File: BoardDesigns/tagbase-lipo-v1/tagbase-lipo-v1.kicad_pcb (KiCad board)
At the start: 2 copper layers, 50.8 x 69.9 mm, 38 parts, among them J1 Conn_01x04_Female, J101 Conn_02x03_Odd_Even, J102 Conn_02x05_Odd_Even, J104 USB_B_Mini, J2 Conn_01x06, J5 Conn_01x02, SW1 SW_SPDT, SW2 SW_SPDT, U1 XC6206P332MR, U105 Tactile Switch, U2 XC6808ANC28R-G, U3 XC6206P182MR, U4 STM32C071GBUx, U5 SN74LVC1T45DCK, U6 SN74LVC1T45DCK

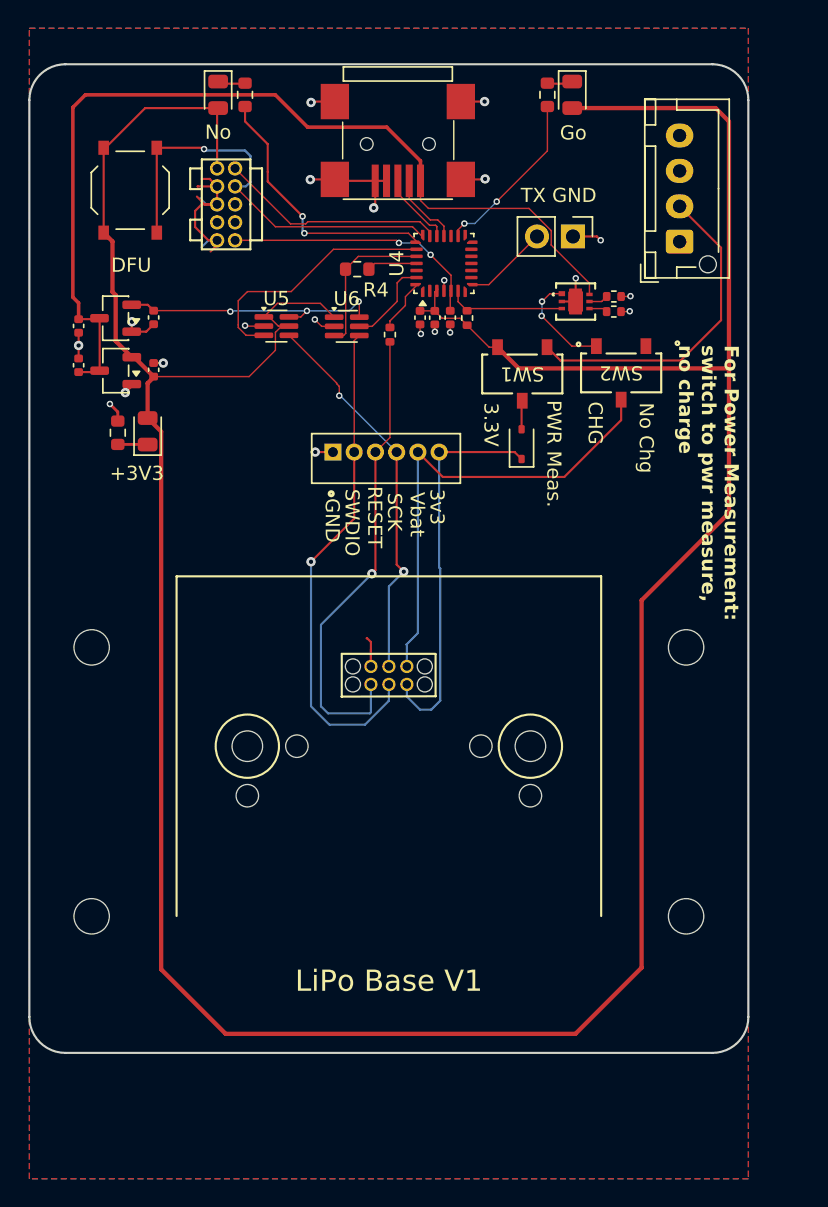
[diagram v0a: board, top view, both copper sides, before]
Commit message: added imutag with bmp581, bitprestag with bmp585
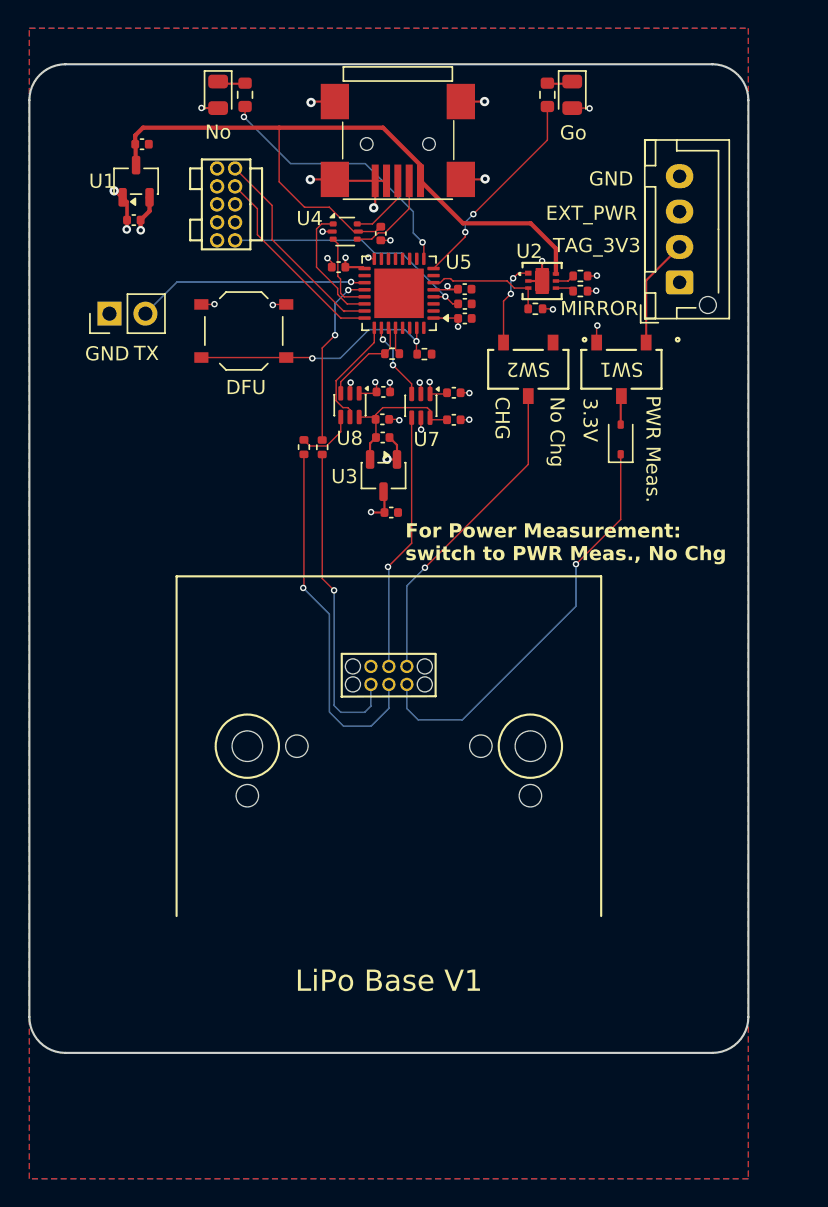
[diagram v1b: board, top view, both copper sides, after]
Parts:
- removed C101: 0.1uF, Capacitor_SMD:C_0402_1005Metric
- removed C6: 4.7uf, Capacitor_SMD:C_0402_1005Metric
- removed D105: LED-GREEN, Diode_SMD:D_0805_2012Metric
- removed H1, H2, H3, H4: MountingHole, MountingHole:MountingHole_2.5mm
- removed J2: Conn_01x06, tagbase:JST_B6B-ZR(LF)(SN)
- removed R5: 100, Resistor_SMD:R_0603_1608Metric
- removed U6: SN74LVC1T45DCK, Package_TO_SOT_SMD:SOT-363_SC-70-6
- added C102: 0.1uF, Capacitor_SMD:C_0402_1005Metric, F.Cu at (126.4, 62.8)
- added C103: 0.1uF, Capacitor_SMD:C_0402_1005Metric, F.Cu at (126.5, 75.9)
- added C109: 0.1uF, Capacitor_SMD:C_0402_1005Metric, F.Cu at (131.6, 75.9)
- added C110: 0.1uF, Capacitor_SMD:C_0402_1005Metric, F.Cu at (131.6, 74.0)
- added C111: 0.1uF, Capacitor_SMD:C_0402_1005Metric, F.Cu at (126.6, 74.0)
- added C3: 0.1uF, Capacitor_SMD:C_0402_1005Metric, F.Cu at (123.4, 65.1)
- added C7: 0.1uF, Capacitor_SMD:C_0402_1005Metric, F.Cu at (132.4, 67.7)
- added C8: 0.1uF, Capacitor_SMD:C_0402_1005Metric, F.Cu at (132.4, 66.7)
- added R105: 12K, Resistor_SMD:R_0402_1005Metric, F.Cu at (129.5, 71.3)
- added R106: 100, Resistor_SMD:R_0402_1005Metric, F.Cu at (121.0, 77.8)
- added U7: SN74LVC1T45DCK, Package_TO_SOT_SMD:SOT-363_SC-70-6, F.Cu at (129.3, 74.9)
- added U8: SN74LVC1T45DCK, Package_TO_SOT_SMD:SOT-363_SC-70-6, F.Cu at (124.2, 74.9)
- R102: value 100 -> 220
- R4: footprint Resistor_SMD:R_0603_1608Metric -> Resistor_SMD:R_0402_1005Metric
- U4: value STM32C071GBUx -> USBLC6-2P6; footprint Package_DFN_QFN:QFN-28_4x4mm_P0.5mm -> Package_TO_SOT_SMD:SOT-666
- U5: value SN74LVC1T45DCK -> STM32L432KBU6; footprint Package_TO_SOT_SMD:SOT-363_SC-70-6 -> Package_DFN_QFN:UFQFPN-32-1EP_5x5mm_P0.5mm_EP3.5x3.5mm
- moved J5 33.2 mm to (107.3, 68.4), turned to 90 degrees
- moved C4 25.7 mm to (127.2, 82.5), turned to 0 degrees
- moved U3 22.0 mm to (126.6, 79.9), turned to -90 degrees
- moved C5 18.3 mm to (126.6, 77.2), turned to 0 degrees
- moved C1 16.2 mm to (109.6, 56.5), turned to 0 degrees
- moved U1 13.5 mm to (109.1, 59.1), turned to 90 degrees
- moved U105 12.8 mm to (116.8, 69.6), turned to 180 degrees
- moved C104 10.7 mm to (109.0, 61.8), turned to 180 degrees
- moved R104 9.29 mm to (122.3, 77.9), turned to -90 degrees
- moved U5 8.97 mm to (127.7, 67.0), turned to 180 degrees
- moved U4 7.33 mm to (123.9, 62.6), turned to 0 degrees
- moved SW1 7.01 mm to (143.4, 72.4)
- moved D1 7.01 mm to (143.4, 77.3)
- moved SW2 6.57 mm to (136.8, 72.4)
- moved R4 6.46 mm to (127.2, 71.2)
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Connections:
- C4 pad 1: VUSB -> +3V3
- J102 pad 10: /NRST -> NRST
- J102 pad 4: /SWCLK -> /SCLK
- R104 pad 1: TAG_RESET -> Net-(U5-PA10)
- R104 pad 2: Net-(U4-PB8) -> TAG_RESET
- R4 pad 1: Net-(U4-PB5) -> Net-(U5-PB5)
- R4 pad 2: Net-(U4-PB4) -> Net-(U5-PB4)
- U105 pad 1: /SWCLK -> /boot0
- U3 pad 3: VUSB -> +3V3
- U4 pad 1: unconnected-(U4-PC14-Pad1) -> /DP
- U4 pad 2: unconnected-(U4-PC15-Pad2) -> GND
- U4 pad 3: +3V3 -> /DM
- U4 pad 4: GND -> /USB_DM
- U4 pad 5: /NRST -> VUSB
- U4 pad 6: /CSO -> /USB_DP
- U5 pad 2: GND -> unconnected-(U5-PC14-Pad2)
- U5 pad 3: Net-(U4-PB3) -> unconnected-(U5-PC15-Pad3)
- U5 pad 4: TAG_SCK -> NRST
- U5 pad 6: +1V8 -> /CSO
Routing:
- net +3V3: track 231.7 -> 23.5 mm, vias 0 -> 14
- net /SWCLK: track 30.7 -> 0.00 mm, vias 1 -> 0
- net GND: track 50.7 -> 29.4 mm
- net /NRST: track 18.8 -> 0.00 mm, vias 2 -> 0
- net NRST: track 0.00 -> 18.5 mm, vias 0 -> 1
- net /boot0: track 0.00 -> 18.3 mm, vias 0 -> 2
- net Net-(U4-PB3): track 18.1 -> 0.00 mm
- net TAG_3V3_IN: track 23.2 -> 7.76 mm
- net VUSB: track 67.3 -> 52.2 mm
- net /SCLK: track 0.00 -> 14.1 mm
- net Net-(U5-PA10): track 0.00 -> 12.5 mm, vias 0 -> 2
- net TAG_VBAT: track 33.7 -> 22.7 mm, vias 0 -> 1
- net TAG_RESET: track 33.4 -> 22.6 mm
- net Net-(U4-PB4): track 10.8 -> 0.00 mm
- net /UART_TX: track 6.11 -> 16.4 mm, vias 0 -> 1
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- added copper zone on In1.Cu, net +3V3
- added copper zone on In2.Cu, net GND
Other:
- copper layers 2 -> 4
- board text added: "For Power Measurement: switch to PWR Meas., No Chg"
- board text added: "Geoffrey Brown 8/8/2026"
- board text removed: "+3V3"
- board text removed: "For Power Measurement: switch to pwr measure, no charge"
- board text removed: "Geoffrey Brown 3/5/2026"
- board text removed: "SCK"

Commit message: added smps breakout board
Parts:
- removed D1: D_Schottky_Small, Diode_SMD:D_SOD-323
- added C6: 0.1uF, Capacitor_SMD:C_0402_1005Metric, F.Cu at (134.5, 73.2)
- added R5: 1M, Resistor_SMD:R_0402_1005Metric, F.Cu at (135.6, 76.5)
- added U6: TLV9001IDCKR, Package_TO_SOT_SMD:SOT-353_SC-70-5, F.Cu at (136.2, 73.7)
- moved SW2 7.95 mm to (141.6, 78.7)
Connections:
- J101 pad 6: TAG_VBAT -> TAG_3V3
- SW1 pad 2: Net-(D1-A) -> Net-(SW1-B)
- SW2 pad 1: unconnected-(SW2-A-Pad1) -> Net-(SW1-B)
- SW2 pad 2: TAG_VBAT -> TAG_3V3
- U5 pad 30: unconnected-(U5-PB7-Pad30) -> /TAG_SCK_EN
- U5 pad 6: /CSO -> /TAG_3V3_Valid
- U5 pad 7: /en1.8v -> /CSO
- U7 pad 5: +3V3 -> /TAG_SCK_EN
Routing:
- net TAG_VBAT: track 22.7 -> 0.00 mm, vias 1 -> 0
- net TAG_3V3: track 29.4 -> 50.0 mm
- net /TAG_3V3_Valid: track 0.00 -> 13.3 mm
- net /TAG_SCK_EN: track 0.00 -> 8.37 mm, vias 0 -> 2
- net /BAT: track 6.04 -> 13.9 mm
- net Net-(SW1-B): track 0.00 -> 2.64 mm
- net GND: track 29.4 -> 31.9 mm, vias 21 -> 26
- net Net-(D1-A): track 2.04 -> 0.00 mm
- net Net-(U6-+): track 0.00 -> 1.51 mm
- net +3V3: track 23.5 -> 24.4 mm
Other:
- board text added: "Chg"
- board text removed: "CHG"

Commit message: checkpoint
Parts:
- U3: value XC6206P182MR -> AP2112K-1.8; footprint Package_TO_SOT_SMD:SOT-23-3 -> Package_TO_SOT_SMD:SOT-23-5
- moved C4 0.95 mm to (126.2, 82.7)
- turned U3 to 90 degrees
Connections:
- U3 pad 1: GND -> +3V3
- U3 pad 2: +1V8 -> GND
- U3 pad 3: +3V3 -> /en1.8v
- U5 pad 29: unconnected-(U5-PB6-Pad29) -> /en1.8v
- U5 pad 30: /TAG_SCK_EN -> unconnected-(U5-PB7-Pad30)
- U7 pad 5: /TAG_SCK_EN -> +3V3
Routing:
- net /en1.8v: track 0.00 -> 13.8 mm, vias 0 -> 2
- net /TAG_SCK_EN: track 8.37 -> 0.00 mm, vias 2 -> 0
- net GND: track 31.9 -> 32.5 mm, vias 26 -> 27
- net +3V3: track 24.4 -> 25.0 mm, vias 14 -> 15
